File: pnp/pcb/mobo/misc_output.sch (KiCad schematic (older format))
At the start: 35 parts, among them J10 MF3, J11 MF4, J12 DOWNWARDS_LIGHT, J13 UPWARDS_LIGHT, J14 5V_INJECTION, J15 RS-485_1, J16 RS-485_2, J17 RS-485_3, J6 SERVO1, J7 SERVO2, J8 MF1, J9 MF2, Q1 IRF540N, Q2 IRF540N, Q3 IRF540N, Q4 IRF540N, U2 SP3485EN, U3 SP3485EN, U4 SP3485EN

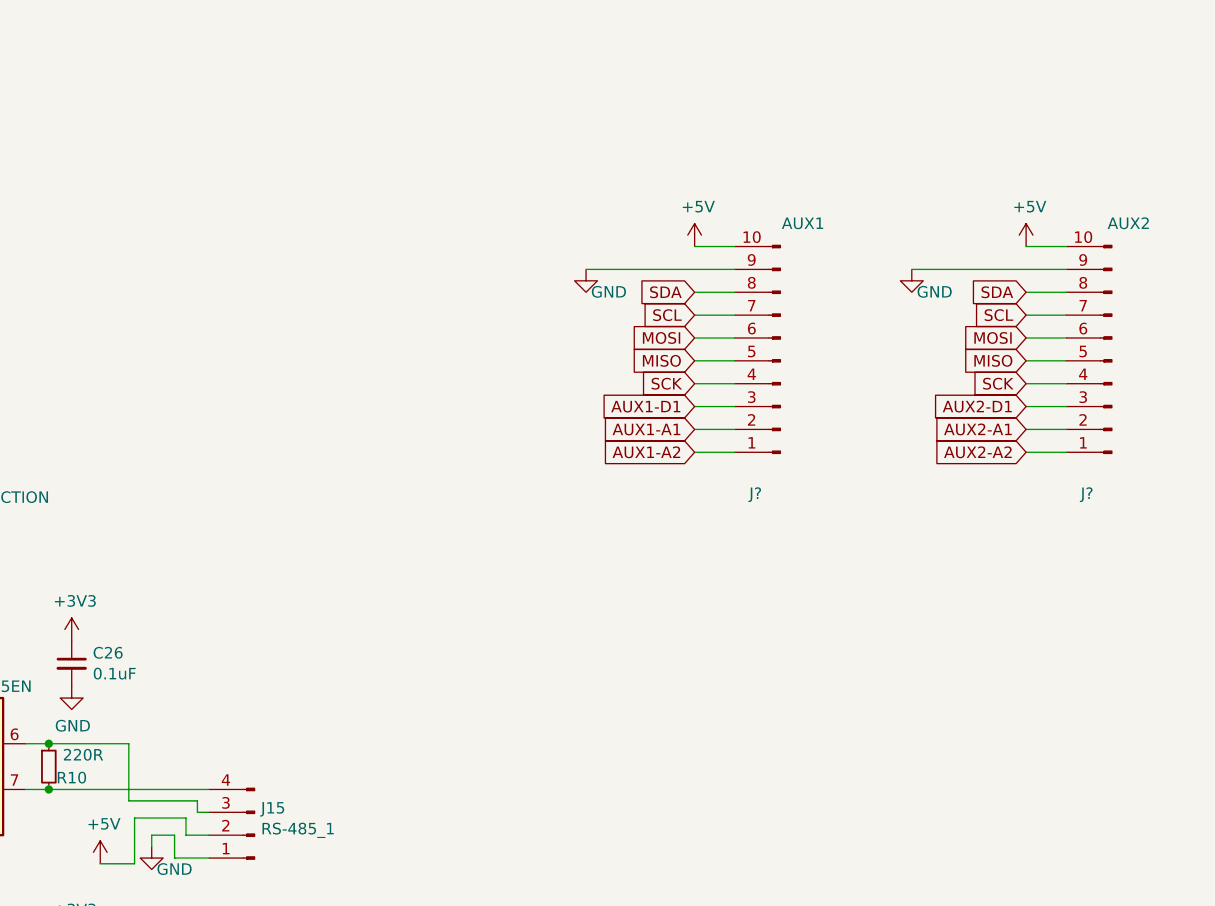
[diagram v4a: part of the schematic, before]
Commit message: added 12v routing to increase current allowed
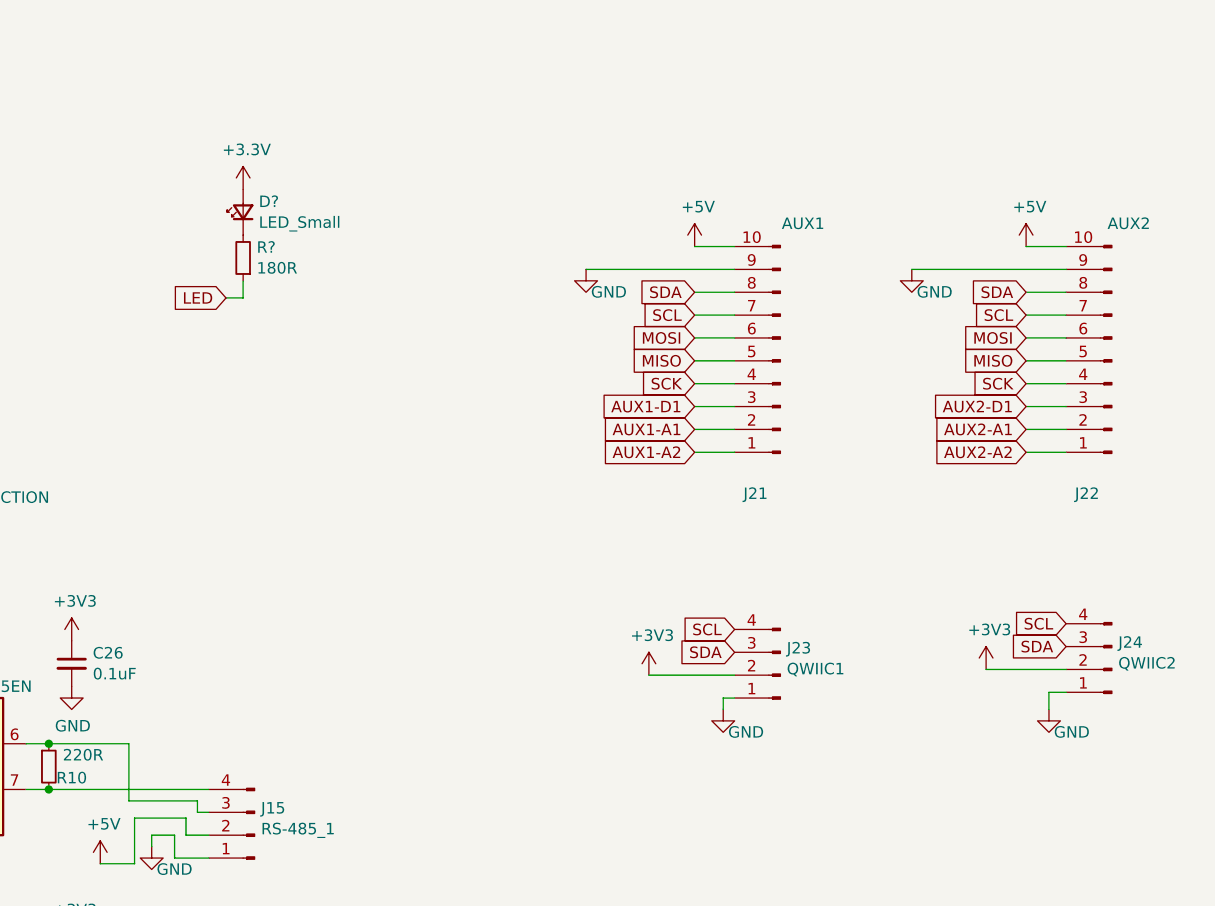
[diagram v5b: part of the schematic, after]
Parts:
- added D?: LED_Small, symbol Device:LED_Small
- added J23: QWIIC1, Connector_JST:JST_SH_BM04B-SRSS-TB_1x04-1MP_P1.00mm_Vertical, symbol Connector:Conn_01x04_Male
- added J24: QWIIC2, Connector_JST:JST_SH_BM04B-SRSS-TB_1x04-1MP_P1.00mm_Vertical, symbol Connector:Conn_01x04_Male
- added R?: 180R, Resistor_SMD:R_0805_2012Metric_Pad1.15x1.40mm_HandSolder, symbol Device:R_Small
- J10, J11, J14, J8, J9: footprint Connector_JST:JST_XH_B2B-XH-A_1x02_P2.50mm_Vertical -> Connector_JST:JST_XH_B02B-XH-A_1x02_P2.50mm_Vertical
- J12, J13, J6, J7: footprint Connector_JST:JST_XH_B3B-XH-A_1x03_P2.50mm_Vertical -> Connector_JST:JST_XH_B03B-XH-A_1x03_P2.50mm_Vertical
- J15, J16, J17: footprint Connector_JST:JST_XH_B4B-XH-A_1x04_P2.50mm_Vertical -> Connector_JST:JST_XH_B04B-XH-A_1x04_P2.50mm_Vertical
- J21, J22: renamed from J?; footprint (none) -> Connector_IDC:IDC-Header_2x05_P2.54mm_Vertical
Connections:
- net +3V3: now also D?.2 (A), J23.2 (Pin_2), J24.2 (Pin_2)
- net GND: now also J23.1 (Pin_1), J24.1 (Pin_1)
- net SCL: now also J23.4 (Pin_4), J24.4 (Pin_4)
- net SDA: now also J23.3 (Pin_3), J24.3 (Pin_3)
- new net: D?.1 (K), R?.2
- new net LED: R?.1
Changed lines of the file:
@@
 F 0 "J6" H 1772 832 50  0000 R CNN
 F 1 "SERVO1" H 1772 923 50  0000 R CNN
-F 2 "Connector_JST:JST_XH_B3B-XH-A_1x03_P2.50mm_Vertical" H 1800 900 50  0001 C CNN
+F 2 "Connector_JST:JST_XH_B03B-XH-A_1x03_P2.50mm_Vertical" H 1800 900 50  0001 C CNN
 F 3 "~" H 1800 900 50  0001 C CNN
 	1    1800 900
@@
 F 0 "J7" H 1772 1432 50  0000 R CNN
 F 1 "SERVO2" H 1772 1523 50  0000 R CNN
-F 2 "Connector_JST:JST_XH_B3B-XH-A_1x03_P2.50mm_Vertical" H 1800 1500 50  0001 C CNN
+F 2 "Connector_JST:JST_XH_B03B-XH-A_1x03_P2.50mm_Vertical" H 1800 1500 50  0001 C CNN
 F 3 "~" H 1800 1500 50  0001 C CNN
 	1    1800 1500
@@
 F 0 "J8" H 2230 2342 50  0000 L CNN
 F 1 "MF1" H 2230 2251 50  0000 L CNN
-F 2 "Connector_JST:JST_XH_B2B-XH-A_1x02_P2.50mm_Vertical" H 2150 2350 50  0001 C CNN
+F 2 "Connector_JST:JST_XH_B02B-XH-A_1x02_P2.50mm_Vertical" H 2150 2350 50  0001 C CNN
 F 3 "~" H 2150 2350 50  0001 C CNN
 	1    2150 2350
@@
 F 0 "J9" H 2230 3742 50  0000 L CNN
 F 1 "MF2" H 2230 3651 50  0000 L CNN
-F 2 "Connector_JST:JST_XH_B2B-XH-A_1x02_P2.50mm_Vertical" H 2150 3750 50  0001 C CNN
+F 2 "Connector_JST:JST_XH_B02B-XH-A_1x02_P2.50mm_Vertical" H 2150 3750 50  0001 C CNN
 F 3 "~" H 2150 3750 50  0001 C CNN
 	1    2150 3750
@@
 F 0 "J10" H 2230 5142 50  0000 L CNN
 F 1 "MF3" H 2230 5051 50  0000 L CNN
-F 2 "Connector_JST:JST_XH_B2B-XH-A_1x02_P2.50mm_Vertical" H 2150 5150 50  0001 C CNN
+F 2 "Connector_JST:JST_XH_B02B-XH-A_1x02_P2.50mm_Vertical" H 2150 5150 50  0001 C CNN
 F 3 "~" H 2150 5150 50  0001 C CNN
 	1    2150 5150
@@
 F 0 "J11" H 2230 6542 50  0000 L CNN
 F 1 "MF4" H 2230 6451 50  0000 L CNN
-F 2 "Connector_JST:JST_XH_B2B-XH-A_1x02_P2.50mm_Vertical" H 2150 6550 50  0001 C CNN
+F 2 "Connector_JST:JST_XH_B02B-XH-A_1x02_P2.50mm_Vertical" H 2150 6550 50  0001 C CNN
 F 3 "~" H 2150 6550 50  0001 C CNN
 	1    2150 6550
@@
 F 0 "J12" H 3622 882 50  0000 R CNN
 F 1 "DOWNWARDS_LIGHT" H 3622 973 50  0000 R CNN
-F 2 "Connector_JST:JST_XH_B3B-XH-A_1x03_P2.50mm_Vertical" H 3650 950 50  0001 C CNN
+F 2 "Connector_JST:JST_XH_B03B-XH-A_1x03_P2.50mm_Vertical" H 3650 950 50  0001 C CNN
 F 3 "~" H 3650 950 50  0001 C CNN
 	1    3650 950
@@
 F 0 "J13" H 3622 1482 50  0000 R CNN
 F 1 "UPWARDS_LIGHT" H 3622 1573 50  0000 R CNN
-F 2 "Connector_JST:JST_XH_B3B-XH-A_1x03_P2.50mm_Vertical" H 3650 1550 50  0001 C CNN
+F 2 "Connector_JST:JST_XH_B03B-XH-A_1x03_P2.50mm_Vertical" H 3650 1550 50  0001 C CNN
 F 3 "~" H 3650 1550 50  0001 C CNN
 	1    3650 1550
@@
 F 0 "J15" H 5622 4132 50  0000 R CNN
 F 1 "RS-485_1" H 5622 4223 50  0000 R CNN
-F 2 "Connector_JST:JST_XH_B4B-XH-A_1x04_P2.50mm_Vertical" H 5650 4250 50  0001 C CNN
+F 2 "Connector_JST:JST_XH_B04B-XH-A_1x04_P2.50mm_Vertical" H 5650 4250 50  0001 C CNN
 F 3 "~" H 5650 4250 50  0001 C CNN
 	1    5650 4250
@@
 F 0 "J14" H 4222 2682 50  0000 R CNN
 F 1 "5V_INJECTION" H 4222 2773 50  0000 R CNN
-F 2 "Connector_JST:JST_XH_B2B-XH-A_1x02_P2.50mm_Vertical" H 4250 2800 50  0001 C CNN
+F 2 "Connector_JST:JST_XH_B02B-XH-A_1x02_P2.50mm_Vertical" H 4250 2800 50  0001 C CNN
 F 3 "~" H 4250 2800 50  0001 C CNN
 	1    4250 2800
@@
 F 0 "J16" H 5622 5482 50  0000 R CNN
 F 1 "RS-485_2" H 5622 5573 50  0000 R CNN
-F 2 "Connector_JST:JST_XH_B4B-XH-A_1x04_P2.50mm_Vertical" H 5650 5600 50  0001 C CNN
+F 2 "Connector_JST:JST_XH_B04B-XH-A_1x04_P2.50mm_Vertical" H 5650 5600 50  0001 C CNN
 F 3 "~" H 5650 5600 50  0001 C CNN
 	1    5650 5600
@@
 F 0 "J17" H 5622 6832 50  0000 R CNN
 F 1 "RS-485_3" H 5622 6923 50  0000 R CNN
-F 2 "Connector_JST:JST_XH_B4B-XH-A_1x04_P2.50mm_Vertical" H 5650 6950 50  0001 C CNN
+F 2 "Connector_JST:JST_XH_B04B-XH-A_1x04_P2.50mm_Vertical" H 5650 6950 50  0001 C CNN
 F 3 "~" H 5650 6950 50  0001 C CNN
 	1    5650 6950
@@
 AUX2-A1
 $Comp
-L Connector:Conn_01x10_Male J?
+L Connector:Conn_01x10_Male J21
 U 1 1 5F9678C9
 P 7950 2175
-F 0 "J?" H 8058 2756 50  0000 C CNN
+F 0 "J21" H 8058 2756 50  0000 C CNN
 F 1 "AUX1" H 7850 1575 50  0000 C CNN
-F 2 "" H 7950 2175 50  0001 C CNN
+F 2 "Connector_IDC:IDC-Header_2x05_P2.54mm_Vertical" H 7950 2175 50  0001 C CNN
 F 3 "~" H 7950 2175 50  0001 C CNN
 	1    7950 2175
@@
 $EndComp
 $Comp
-L power:+5V #PWR?
+L power:+5V #PWR0196
 U 1 1 5F9685BF
 P 7575 1675
-F 0 "#PWR?" H 7575 1525 50  0001 C CNN
+F 0 "#PWR0196" H 7575 1525 50  0001 C CNN
 F 1 "+5V" H 7590 1848 50  0000 C CNN
 F 2 "" H 7575 1675 50  0001 C CNN
@@
 $EndComp
 $Comp
-L power:GND #PWR?
+L power:GND #PWR0197
 U 1 1 5F969005
 P 7100 1775
-F 0 "#PWR?" H 7100 1525 50  0001 C CNN
+F 0 "#PWR0197" H 7100 1525 50  0001 C CNN
 F 1 "GND" H 7200 1675 50  0000 C CNN
 F 2 "" H 7100 1775 50  0001 C CNN
@@
 SCK
 $Comp
-L Connector:Conn_01x10_Male J?
+L Connector:Conn_01x10_Male J22
 U 1 1 5F97497A
 P 9400 2175
-F 0 "J?" H 9508 2756 50  0000 C CNN
+F 0 "J22" H 9508 2756 50  0000 C CNN
 F 1 "AUX2" H 9325 1575 50  0000 C CNN
-F 2 "" H 9400 2175 50  0001 C CNN
+F 2 "Connector_IDC:IDC-Header_2x05_P2.54mm_Vertical" H 9400 2175 50  0001 C CNN
 F 3 "~" H 9400 2175 50  0001 C CNN
 	1    9400 2175
@@
 SCK
 $Comp
-L power:GND #PWR?
+L power:GND #PWR0200
 U 1 1 5F97E813
 P 8525 1775
-F 0 "#PWR?" H 8525 1525 50  0001 C CNN
+F 0 "#PWR0200" H 8525 1525 50  0001 C CNN
 F 1 "GND" H 8625 1675 50  0000 C CNN
 F 2 "" H 8525 1775 50  0001 C CNN
@@
 $EndComp
 $Comp
-L power:+5V #PWR?
+L power:+5V #PWR0201
 U 1 1 5F97ED14
 P 9025 1675
-F 0 "#PWR?" H 9025 1525 50  0001 C CNN
+F 0 "#PWR0201" H 9025 1525 50  0001 C CNN
 F 1 "+5V" H 9040 1848 50  0000 C CNN
 F 2 "" H 9025 1675 50  0001 C CNN
@@
 Wire Wire Line
 	9200 2575 9025 2575
+$Comp
+L Connector:Conn_01x04_Male J23
+U 1 1 5FA31EAD
+P 7950 3550
+F 0 "J23" H 7922 3432 50  0000 R CNN
+F 1 "QWIIC1" H 7922 3523 50  0000 R CNN
+F 2 "Connector_JST:JST_SH_BM04B-SRSS-TB_1x04-1MP_P1.00mm_Vertical" H 7950 3550 50  0001 C CNN
+F 3 "~" H 7950 3550 50  0001 C CNN
+	1    7950 3550
+	-1   0    0    1
+$EndComp
+$Comp
+L Connector:Conn_01x04_Male J24
+U 1 1 5FA326C9
+P 9400 3525
+F 0 "J24" H 9372 3407 50  0000 R CNN
+F 1 "QWIIC2" H 9372 3498 50  0000 R CNN
+F 2 "Connector_JST:JST_SH_BM04B-SRSS-TB_1x04-1MP_P1.00mm_Vertical" H 9400 3525 50  0001 C CNN
+F 3 "~" H 9400 3525 50  0001 C CNN
+	1    9400 3525
+	-1   0    0    1
+$EndComp
+$Comp
+L power:GND #PWR0178
+U 1 1 5FA33418
+P 7700 3700
+F 0 "#PWR0178" H 7700 3450 50  0001 C CNN
+F 1 "GND" H 7800 3600 50  0000 C CNN
+F 2 "" H 7700 3700 50  0001 C CNN
+F 3 "" H 7700 3700 50  0001 C CNN
+	1    7700 3700
+	1    0    0    -1
+$EndComp
+Text GLabel 7750 3450 0    50   Input ~ 0
+SDA
+Text GLabel 7750 3350 0    50   Input ~ 0
+SCL
+Wire Wire Line
+	7700 3700 7700 3650
+Wire Wire Line
+	7700 3650 7750 3650
+Wire Wire Line
+	7375 3550 7750 3550
+Text GLabel 9200 3425 0    50   Input ~ 0
+SDA
+Text GLabel 9200 3325 0    50   Input ~ 0
+SCL
+$Comp
+L power:GND #PWR0179
+U 1 1 5FA3C02E
+P 9125 3700
+F 0 "#PWR0179" H 9125 3450 50  0001 C CNN
+F 1 "GND" H 9225 3600 50  0000 C CNN
+F 2 "" H 9125 3700 50  0001 C CNN
+F 3 "" H 9125 3700 50  0001 C CNN
+	1    9125 3700
+	1    0    0    -1
+$EndComp
+Wire Wire Line
+	9125 3700 9125 3625
+Wire Wire Line
+	9125 3625 9200 3625
+Wire Wire Line
+	9200 3525 8850 3525
+$Comp
+L power:+3V3 #PWR0202
+U 1 1 5FA44895
+P 7375 3550
+F 0 "#PWR0202" H 7375 3400 50  0001 C CNN
+F 1 "+3V3" H 7390 3723 50  0000 C CNN
+F 2 "" H 7375 3550 50  0001 C CNN
+F 3 "" H 7375 3550 50  0001 C CNN
+	1    7375 3550
+	1    0    0    -1
+$EndComp
+$Comp
+L power:+3V3 #PWR0204
+U 1 1 5FA48C88
+P 8850 3525
+F 0 "#PWR0204" H 8850 3375 50  0001 C CNN
+F 1 "+3V3" H 8865 3698 50  0000 C CNN
+F 2 "" H 8850 3525 50  0001 C CNN
+F 3 "" H 8850 3525 50  0001 C CNN
+	1    8850 3525
+	1    0    0    -1
+$EndComp
+$Comp
+L Device:R_Small R?
+U 1 1 5FA66FB8
+P 5600 1725
+F 0 "R?" H 5541 1679 50  0000 R CNN
+F 1 "180R" H 5541 1770 50  0000 R CNN
+F 2 "Resistor_SMD:R_0805_2012Metric_Pad1.15x1.40mm_HandSolder" H 5600 1725 50  0001 C CNN
+F 3 "~" H 5600 1725 50  0001 C CNN
+	1    5600 1725
+	-1   0    0    1
+$EndComp
+$Comp
+L Device:LED_Small D?
+U 1 1 5FA6A940
+P 5600 1525
+F 0 "D?" V 5646 1457 50  0000 R CNN
+F 1 "LED_Small" V 5555 1457 50  0000 R CNN
+F 2 "" V 5600 1525 50  0001 C CNN
+F 3 "~" V 5600 1525 50  0001 C CNN
+	1    5600 1525
+	0    -1   -1   0
+$EndComp
+Text GLabel 5525 1900 0    50   Input ~ 0
+LED
+$Comp
+L power:+3.3V #PWR?
+U 1 1 5FA75D3F
+P 5600 1425
+F 0 "#PWR?" H 5600 1275 50  0001 C CNN
+F 1 "+3.3V" H 5615 1598 50  0000 C CNN
+F 2 "" H 5600 1425 50  0001 C CNN
+F 3 "" H 5600 1425 50  0001 C CNN
+	1    5600 1425
+	1    0    0    -1
+$EndComp
+Wire Wire Line
+	5525 1900 5600 1900
+Wire Wire Line
+	5600 1900 5600 1825
 $EndSCHEMATC

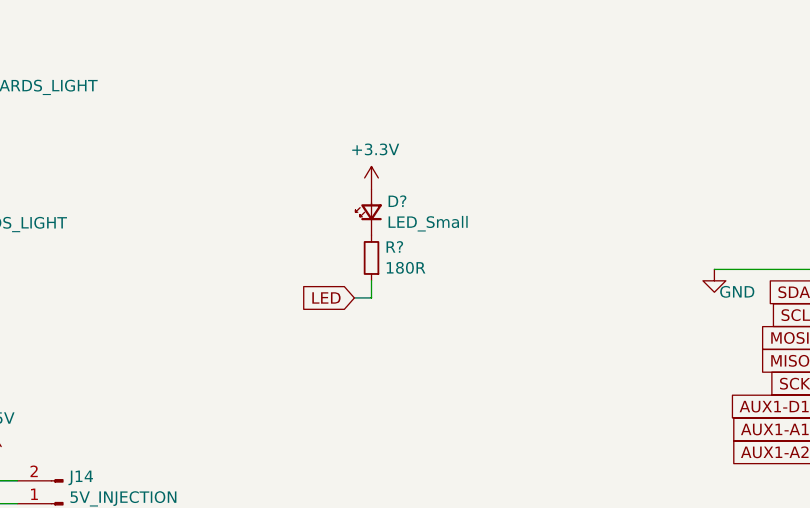
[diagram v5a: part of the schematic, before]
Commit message: usb routing mostly redone
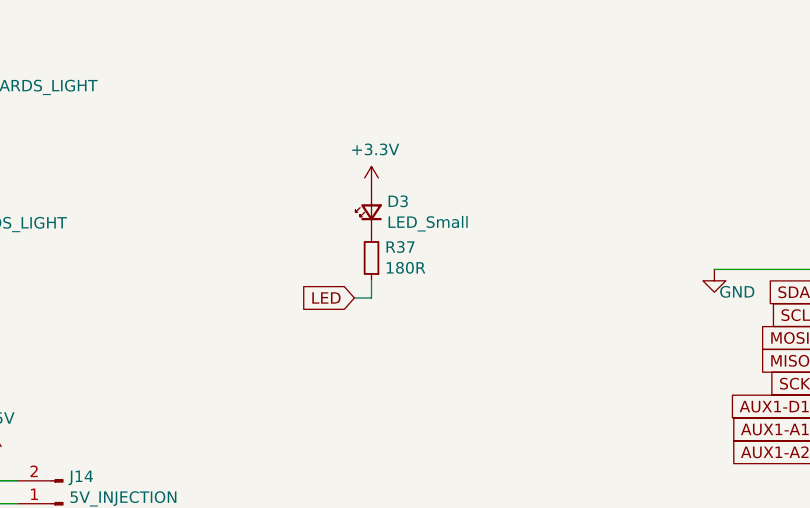
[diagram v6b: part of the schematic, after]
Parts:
- D3: renamed from D?; footprint (none) -> LED_SMD:LED_0805_2012Metric
- gave numbers to parts that had none: 1
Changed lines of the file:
@@
 $EndComp
 $Comp
-L Device:R_Small R?
+L Device:R_Small R37
 U 1 1 5FA66FB8
 P 5600 1725
-F 0 "R?" H 5541 1679 50  0000 R CNN
+F 0 "R37" H 5541 1679 50  0000 R CNN
 F 1 "180R" H 5541 1770 50  0000 R CNN
 F 2 "Resistor_SMD:R_0805_2012Metric_Pad1.15x1.40mm_HandSolder" H 5600 1725 50  0001 C CNN
@@
 $EndComp
 $Comp
-L Device:LED_Small D?
+L Device:LED_Small D3
 U 1 1 5FA6A940
 P 5600 1525
-F 0 "D?" V 5646 1457 50  0000 R CNN
+F 0 "D3" V 5646 1457 50  0000 R CNN
 F 1 "LED_Small" V 5555 1457 50  0000 R CNN
-F 2 "" V 5600 1525 50  0001 C CNN
+F 2 "LED_SMD:LED_0805_2012Metric" V 5600 1525 50  0001 C CNN
 F 3 "~" V 5600 1525 50  0001 C CNN
 	1    5600 1525
@@
 LED
 $Comp
-L power:+3.3V #PWR?
+L power:+3.3V #PWR0206
 U 1 1 5FA75D3F
 P 5600 1425
-F 0 "#PWR?" H 5600 1275 50  0001 C CNN
+F 0 "#PWR0206" H 5600 1275 50  0001 C CNN
 F 1 "+3.3V" H 5615 1598 50  0000 C CNN
 F 2 "" H 5600 1425 50  0001 C CNN

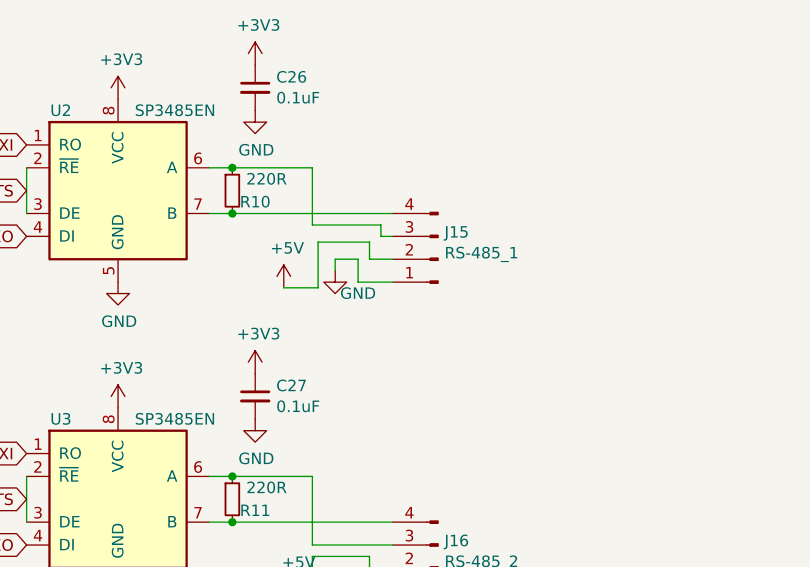
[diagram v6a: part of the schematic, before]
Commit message: finished up routing. still need to add bias resistors to the i2c lines, redo all the connector labels and organize component labels
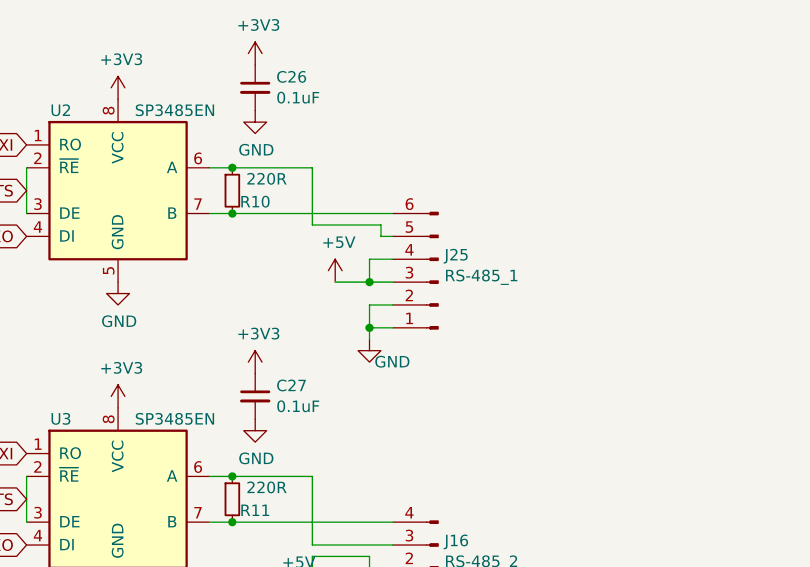
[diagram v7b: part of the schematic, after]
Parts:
- removed J15: RS-485_1, Connector_JST:JST_XH_B04B-XH-A_1x04_P2.50mm_Vertical, symbol Connector:Conn_01x04_Male
- added J25: RS-485_1, Connector_IDC:IDC-Header_2x03_P2.54mm_Vertical, symbol Connector:Conn_01x06_Male
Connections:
- net +5V: now also J25.3 (Pin_3), J25.4 (Pin_4)
- net GND: now also J25.1 (Pin_1), J25.2 (Pin_2)
- net at R10.1, U2.6 (A): now also J25.5 (Pin_5)
- net at R10.2, U2.7 (B): now also J25.6 (Pin_6)
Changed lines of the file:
@@
 Wire Wire Line
 	3850 6550 3850 6750
-$Comp
-L Connector:Conn_01x04_Male J15
-U 1 1 5F1B00EB
-P 5650 4250
-F 0 "J15" H 5622 4132 50  0000 R CNN
-F 1 "RS-485_1" H 5622 4223 50  0000 R CNN
-F 2 "Connector_JST:JST_XH_B04B-XH-A_1x04_P2.50mm_Vertical" H 5650 4250 50  0001 C CNN
-F 3 "~" H 5650 4250 50  0001 C CNN
-	1    5650 4250
-	-1   0    0    1
-$EndComp
 Wire Wire Line
 	4650 3850 4750 3850
@@
 L power:GND #PWR0155
 U 1 1 5F1B543F
-P 5200 4300
-F 0 "#PWR0155" H 5200 4050 50  0001 C CNN
-F 1 "GND" H 5300 4200 50  0000 C CNN
-F 2 "" H 5200 4300 50  0001 C CNN
-F 3 "" H 5200 4300 50  0001 C CNN
-	1    5200 4300
-	1    0    0    -1
-$EndComp
-Wire Wire Line
-	5200 4300 5200 4250
-Wire Wire Line
-	5200 4250 5300 4250
-Wire Wire Line
-	5300 4250 5300 4350
-Wire Wire Line
-	5300 4350 5450 4350
+P 5350 4600
+F 0 "#PWR0155" H 5350 4350 50  0001 C CNN
+F 1 "GND" H 5450 4500 50  0000 C CNN
+F 2 "" H 5350 4600 50  0001 C CNN
+F 3 "" H 5350 4600 50  0001 C CNN
+	1    5350 4600
+	1    0    0    -1
+$EndComp
 Wire Wire Line
 	5450 4250 5350 4250
-$Comp
-L power:+5V #PWR0156
-U 1 1 5F15768C
-P 4975 4375
-F 0 "#PWR0156" H 4975 4225 50  0001 C CNN
-F 1 "+5V" H 4990 4548 50  0000 C CNN
-F 2 "" H 4975 4375 50  0001 C CNN
-F 3 "" H 4975 4375 50  0001 C CNN
-	1    4975 4375
-	1    0    0    -1
-$EndComp
 $Comp
 L power:+5V #PWR0157
@@
 485_3_RTS
 Wire Wire Line
-	5350 4250 5350 4175
-Wire Wire Line
-	5350 4175 5125 4175
-Wire Wire Line
-	5125 4175 5125 4375
-Wire Wire Line
-	5125 4375 4975 4375
-Wire Wire Line
 	4750 5400 5450 5400
 Wire Wire Line
@@
 Wire Wire Line
 	5600 1900 5600 1825
+$Comp
+L Connector:Conn_01x06_Male J25
+U 1 1 5F9E6EE4
+P 5650 4350
+F 0 "J25" H 5622 4232 50  0000 R CNN
+F 1 "RS-485_1" H 5622 4323 50  0000 R CNN
+F 2 "Connector_IDC:IDC-Header_2x03_P2.54mm_Vertical" H 5650 4350 50  0001 C CNN
+F 3 "~" H 5650 4350 50  0001 C CNN
+	1    5650 4350
+	-1   0    0    1
+$EndComp
+Wire Wire Line
+	5350 4600 5350 4550
+Wire Wire Line
+	5350 4450 5450 4450
+Wire Wire Line
+	5450 4550 5350 4550
+Connection ~ 5350 4550
+Wire Wire Line
+	5350 4550 5350 4450
+$Comp
+L power:+5V #PWR0156
+U 1 1 5F15768C
+P 5200 4350
+F 0 "#PWR0156" H 5200 4200 50  0001 C CNN
+F 1 "+5V" H 5215 4523 50  0000 C CNN
+F 2 "" H 5200 4350 50  0001 C CNN
+F 3 "" H 5200 4350 50  0001 C CNN
+	1    5200 4350
+	1    0    0    -1
+$EndComp
+Wire Wire Line
+	5200 4350 5350 4350
+Wire Wire Line
+	5350 4250 5350 4350
+Connection ~ 5350 4350
+Wire Wire Line
+	5350 4350 5450 4350
 $EndSCHEMATC
